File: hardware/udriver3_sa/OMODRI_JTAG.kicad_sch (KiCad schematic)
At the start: 2 parts, among them J9 SAMTEC_CLP_02x04_SMD

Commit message: Update some reference on uOmodri V3.1 for fab. Update uOmodri_SA V1.0 reducing heights of top layers components.
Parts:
- J9: footprint udriver3:PinSocket_2x04_P1.27mm_SMD_Vertical -> udriver3:SAMTEC_CLP-104-02-L-D-BE
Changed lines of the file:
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@@
 			)
 		)
-		(property "Footprint" "udriver3:PinSocket_2x04_P1.27mm_SMD_Vertical"
+		(property "Footprint" "udriver3:SAMTEC_CLP-104-02-L-D-BE"
 			(at 144.78 100.33 0)
 			(effects

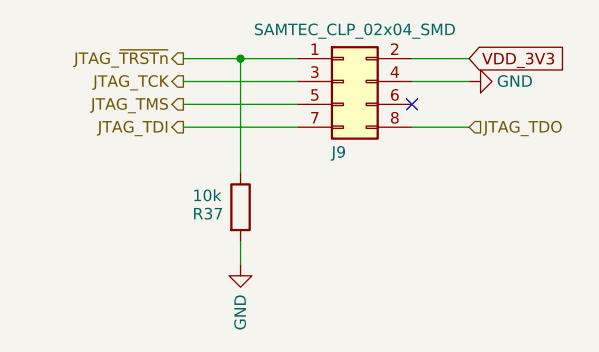
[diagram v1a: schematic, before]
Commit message: Update on uOmodri_SA. Remove USB, com SPI & debug connectors for integration into Myactuator motors. Connectors replaced by a ZIF connector.
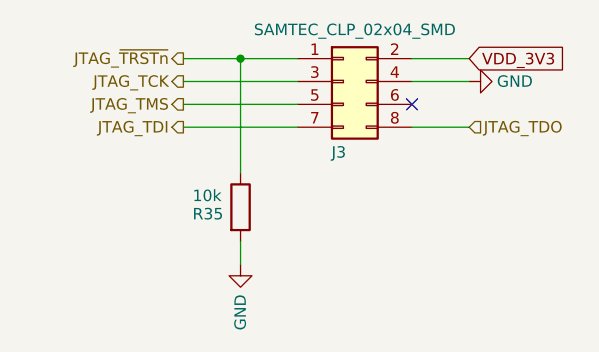
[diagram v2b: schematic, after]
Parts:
- renumbered J9 to J3, R37 to R35
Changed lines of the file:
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@@
 	(title_block
 		(title "Open MOtor DRiver Initiative  - Single Axis (OMODRI_SA)")
-		(date "2024-03-20")
+		(date "2024-11-08")
 		(rev "1.0")
 		(company "LAAS/CNRS")
@@
 		(on_board yes)
 		(dnp no)
-		(property "Reference" "R37"
+		(property "Reference" "R35"
 			(at 128.016 115.062 0)
 			(effects
@@
 			(project "omodri_sa_laas"
 				(path "/de5b13f0-933a-4c4d-9979-13dc57b13241/8971aee4-c199-4562-824f-9b9a5f7ff02d"
-					(reference "R37")
+					(reference "R35")
 					(unit 1)
 				)
@@
 		(on_board yes)
 		(dnp no)
-		(property "Reference" "J9"
+		(property "Reference" "J3"
 			(at 144.272 108.204 0)
 			(effects
@@
 			(project "omodri_sa_laas"
 				(path "/de5b13f0-933a-4c4d-9979-13dc57b13241/8971aee4-c199-4562-824f-9b9a5f7ff02d"
-					(reference "J9")
+					(reference "J3")
 					(unit 1)
 				)
@@
 		(on_board yes)
 		(dnp no)
-		(property "Reference" "#PWR0112"
+		(property "Reference" "#PWR099"
 			(at 165.1 100.33 0)
 			(effects
@@
 			(project "omodri_sa_laas"
 				(path "/de5b13f0-933a-4c4d-9979-13dc57b13241/8971aee4-c199-4562-824f-9b9a5f7ff02d"
-					(reference "#PWR0112")
+					(reference "#PWR099")
 					(unit 1)
 				)
@@
 		(on_board yes)
 		(dnp no)
-		(property "Reference" "#PWR0113"
+		(property "Reference" "#PWR0100"
 			(at 133.35 127 0)
 			(effects
@@
 			(project "omodri_sa_laas"
 				(path "/de5b13f0-933a-4c4d-9979-13dc57b13241/8971aee4-c199-4562-824f-9b9a5f7ff02d"
-					(reference "#PWR0113")
+					(reference "#PWR0100")
 					(unit 1)
 				)
